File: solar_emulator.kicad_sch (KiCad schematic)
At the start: 0 parts

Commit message: partial implementation of schematic includes USB, LEDs for debugging, button for EN, BOOT and regulator to convert 5V to 3.3V from UBC need to implement pin/connector and motor driver
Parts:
- added C1, C4: 100n, symbol Device:C
- added C2: 10u, symbol Device:C
- added C3: 22u, symbol Device:C
- added C5: 1u, symbol Device:C
- added D1: RED, symbol Device:LED
- added D2: GREEN, symbol Device:LED
- added D3, D4: BLUE, symbol Device:LED
- added J1: USB_C_Receptacle, SparkFun-Connector:USB-C_16, symbol SparkFun-Connector:USB_C_Receptacle
- added R1, R3, R4, R5, R6: R, symbol Device:R
- added R2: 5.1k, symbol Device:R
- added R7: 10k, symbol Device:R
- added SW1, SW2: SW_Push, symbol Switch:SW_Push
- added U1: ESP32-S3-WROOM-1, PCM_Espressif:ESP32-S3-WROOM-1, symbol PCM_Espressif:ESP32-S3-WROOM-1
- added U2: LD1117S33TR_SOT223, Package_TO_SOT_SMD:SOT-223-3_TabPin2, symbol Regulator_Linear:LD1117S33TR_SOT223
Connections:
- new net: J1.B5 (CC2), R1.1
- new net: D1.2 (A), R3.2
- new net: D3.2 (A), R5.2
- new net: D4.2 (A), R6.2
- new net: D2.2 (A), R4.2
- new net: J1.A5 (CC1), R2.1
- new net +3V3: C2.1, C3.1, C4.1, R4.1, U1.2 (3V3), U2.2 (VO)
- new net 5V: C1.1, J1.VBUS, R3.1, U2.3 (VI)
- new net D+: J1.A6 (D+), J1.B6 (D+), U1.14 (GPIO20/U1CTS/ADC2_CH9/CLK_OUT1/USB_D+)
- new net D-: J1.A7 (D-), J1.B7 (D-), U1.13 (GPIO19/U1RTS/ADC2_CH8/CLK_OUT2/USB_D-)
- new net EN: C5.1, R7.2, SW2.1, U1.3 (EN)
- new net GND: C1.2, C2.2, C3.2, C4.2, C5.2, D1.1 (K), D2.1 (K), D3.1 (K), D4.1 (K), J1.GND, J1.S (SHIELD), R1.2, R2.2, SW1.2, SW2.2, U1.1 (GND), U1.40 (GND), U1.41 (GND), U2.1 (GND)
- new net GPIO0: SW1.1, U1.27 (GPIO0/BOOT)
- new net GPIO1: R5.1, U1.39 (GPIO1/TOUCH1/ADC1_CH0)
- new net GPIO2: R6.1, U1.38 (GPIO2/TOUCH2/ADC1_CH1)
- new net GPIO3: U1.15 (GPIO3/TOUCH3/ADC1_CH2)
- new net GPIO4: U1.4 (GPIO4/TOUCH4/ADC1_CH3)
- new net GPIO5: U1.5 (GPIO5/TOUCH5/ADC1_CH4)
- new net GPIO6: U1.6 (GPIO6/TOUCH6/ADC1_CH5)
- no-connect marks 0 -> 27

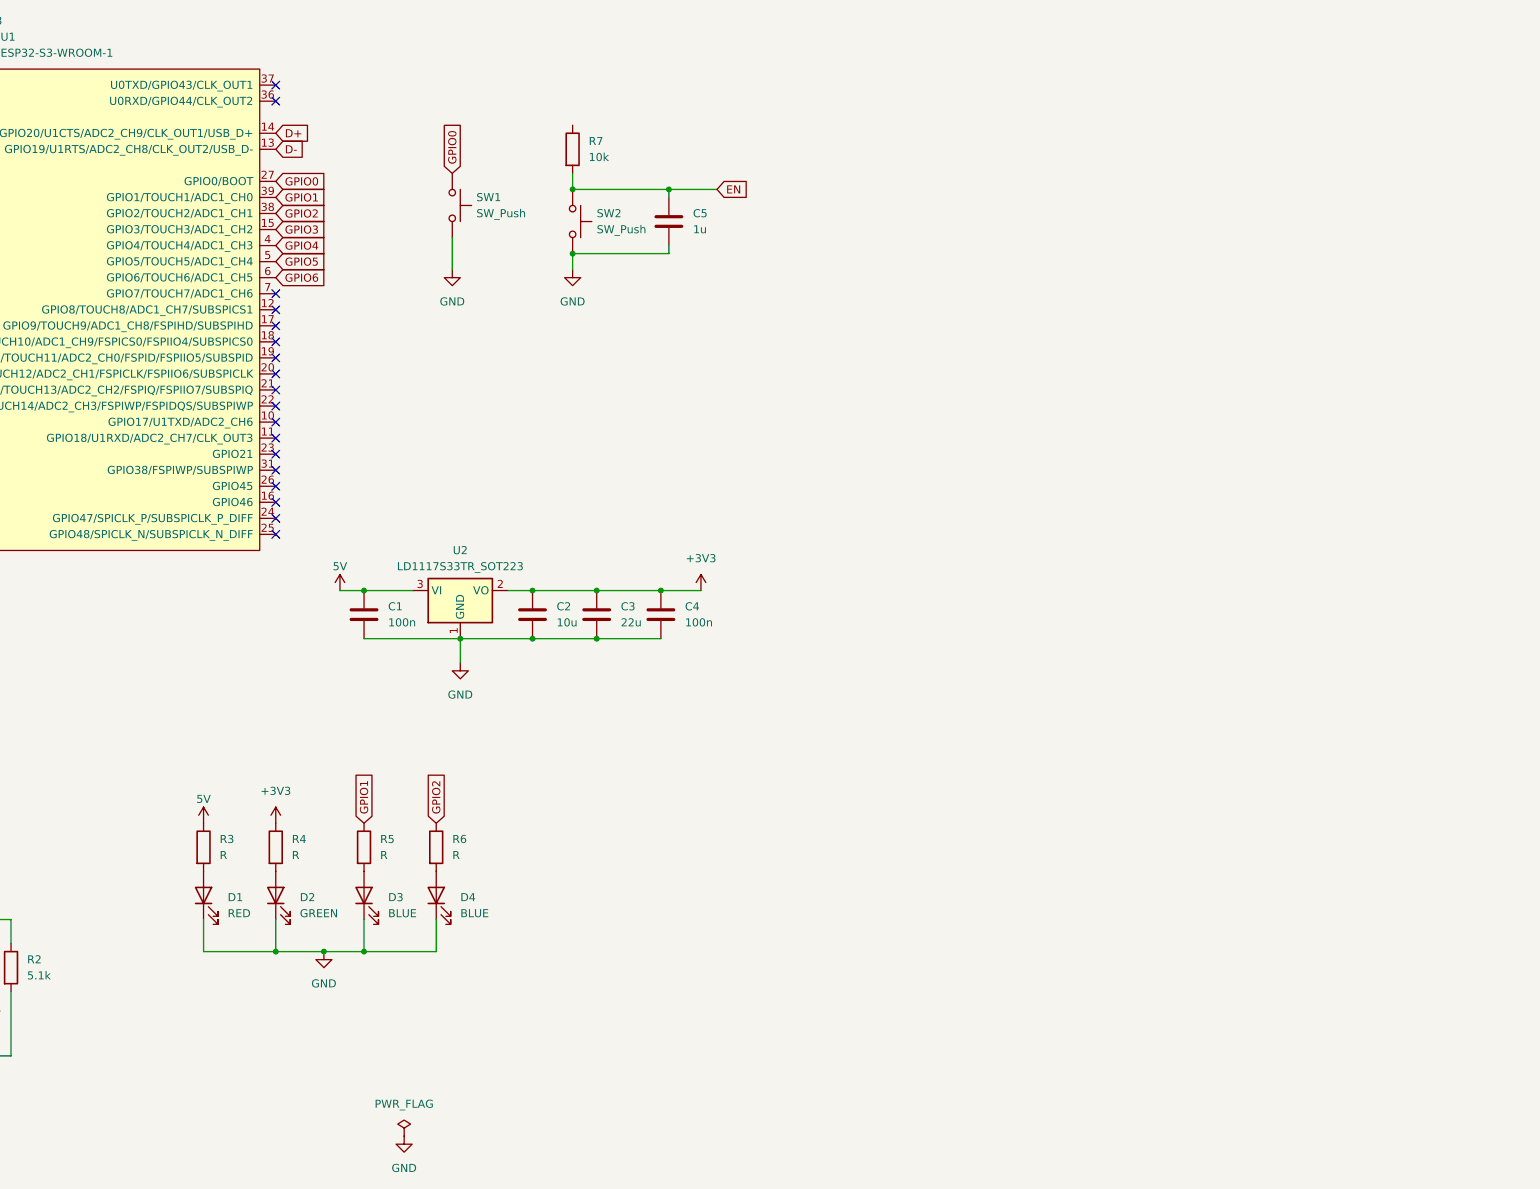
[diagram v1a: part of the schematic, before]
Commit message: Partial impl of motor driver sch
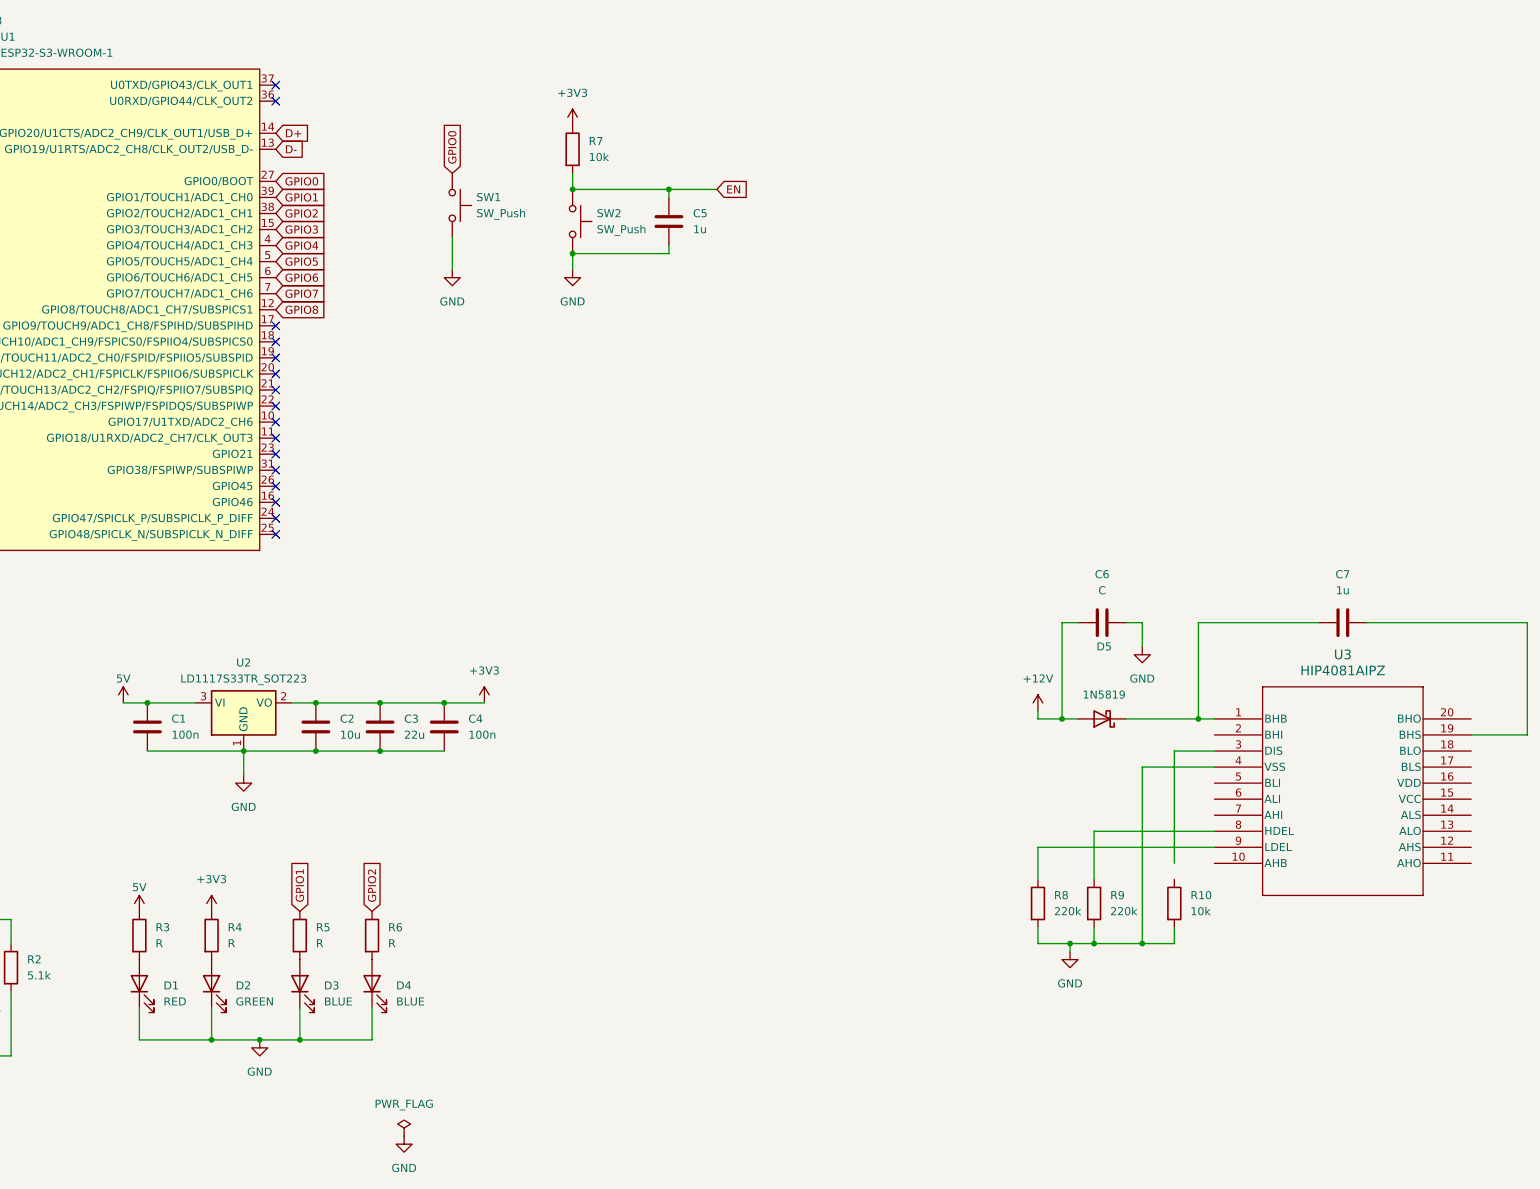
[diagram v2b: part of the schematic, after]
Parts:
- added C6: C, symbol Device:C
- added C7: 1u, symbol Device:C
- added D5: 1N5819, Diode_THT:D_DO-41_SOD81_P10.16mm_Horizontal, symbol Diode:1N5819
- added R10: 10k, symbol Device:R
- added R8, R9: 220k, symbol Device:R
- added U3: HIP4081AIPZ, PDIP20_7P11X26P9_INR, symbol custom_lib:HIP4081AIPZ
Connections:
- net +3V3: now also R7.1
- net GND: now also C6.2, R10.2, R8.2, R9.2, U3.4 (VSS)
- net GPIO8: now reaches U1.12 (GPIO8/TOUCH8/ADC1_CH7/SUBSPICS1)
- net GPIO7: now reaches U1.7 (GPIO7/TOUCH7/ADC1_CH6)
- new net: C7.1, D5.1 (K), U3.1 (BHB)
- new net: C7.2, U3.19 (BHS)
- new net: R9.1, U3.8 (HDEL)
- new net: R8.1, U3.9 (LDEL)
- new net +12V: C6.1, D5.2 (A)
- no-connect marks 27 -> 25
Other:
- moved on the sheet: C1, C2, C3, C4, D1, D2, D3, D4, R3, R4, R5, R6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

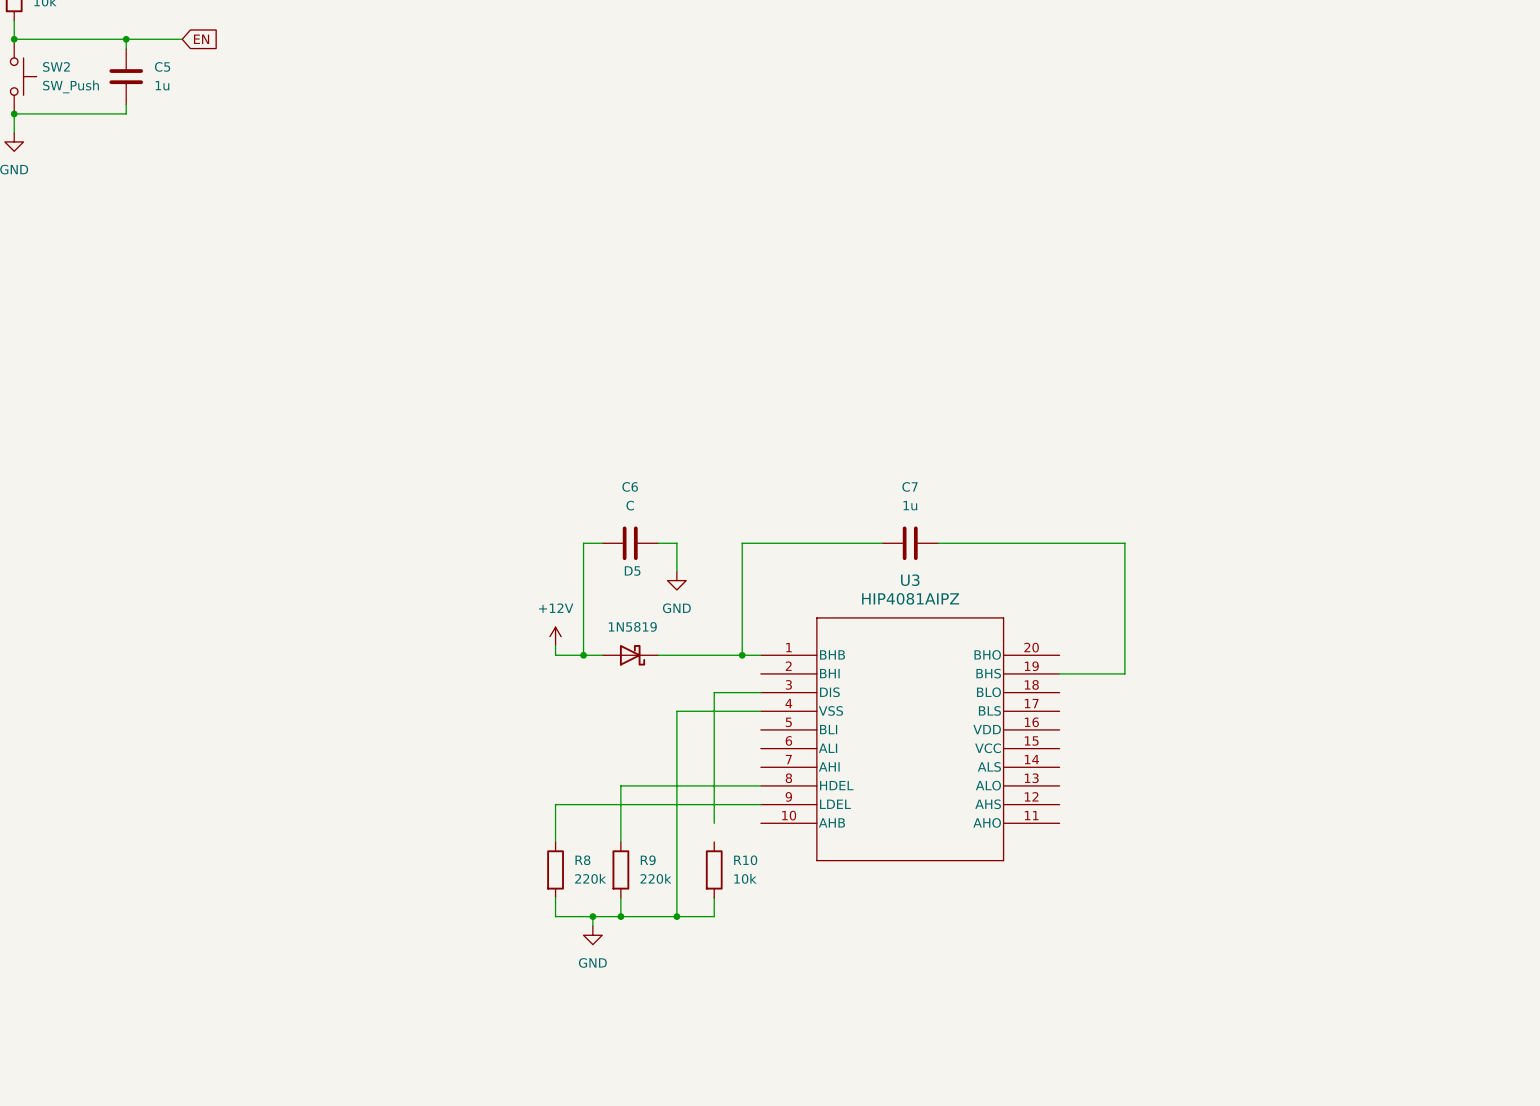
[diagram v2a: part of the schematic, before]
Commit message: Implement one h-bridge circuit
Need to implement another because 4-pin stepper motor
Also need to use ERC to before proceeding w/ pcb
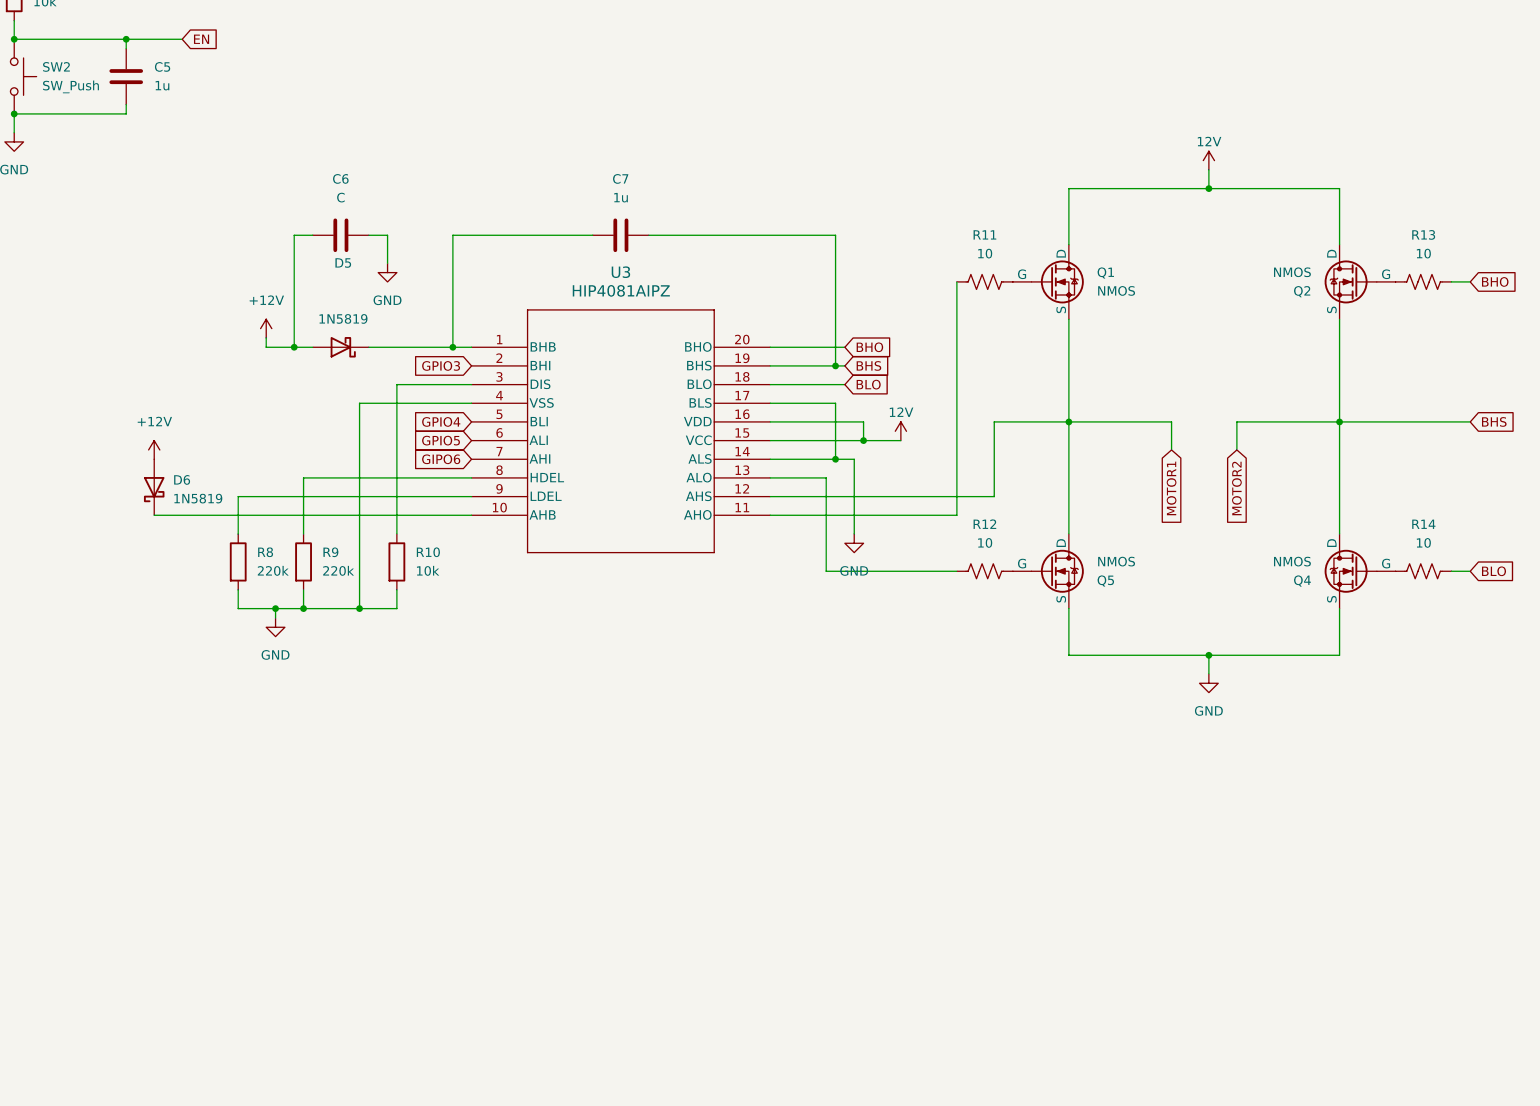
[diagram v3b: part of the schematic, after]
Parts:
- added D6: 1N5819, Diode_THT:D_DO-41_SOD81_P10.16mm_Horizontal, symbol Diode:1N5819
- added Q1, Q2, Q4, Q5: NMOS, symbol Simulation_SPICE:NMOS
- added R11, R12, R13, R14: 10, SparkFun-Resistor:R_0603_1608Metric, symbol SparkFun-Resistor:R
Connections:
- net +12V: now also D6.2 (A)
- net GND: now also U3.14 (ALS), U3.17 (BLS), Q4.3 (S), Q5.3 (S)
- net GPIO3: now also U3.2 (BHI)
- net GPIO4: now also U3.5 (BLI)
- net GPIO5: now also U3.6 (ALI)
- net at U3.10 (AHB): now also D6.1 (K)
- net at U3.11 (AHO): now also R11.2
- net MOTOR1: now reaches U3.12 (AHS)
- net MOTOR1: now also Q1.3 (S), Q5.1 (D)
- net at U3.13 (ALO): now also R12.2
- net 12V: now reaches U3.15 (VCC)
- net 12V: now also U3.16 (VDD), Q1.1 (D), Q2.1 (D)
- net BLO: now reaches U3.18 (BLO)
- net BLO: now also R14.1
- net BHS: now reaches C7.2, U3.19 (BHS)
- net BHS: now also Q2.3 (S), Q4.1 (D)
- net BHO: now reaches U3.20 (BHO)
- net BHO: now also R13.1
- net at U3.3 (DIS): now also R10.1
- net GIPO6: now reaches U3.7 (AHI)
- new net: Q1.2 (G), R11.1
- new net: Q5.2 (G), R12.1
- new net: Q4.2 (G), R14.2
- new net: Q2.2 (G), R13.2
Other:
- moved on the sheet: C6, C7, D5, R10, R8, R9, U3
